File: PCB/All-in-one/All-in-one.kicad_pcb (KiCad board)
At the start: 4 copper layers, 61.9 x 55.5 mm, 81 parts, among them J1 HIGH VOLTAGE, J10 SWD, J2 LOW VOLTAGE, J3 Micro_SD_Card_Det, J4 USB_C_Receptacle_USB2.0, J5 GPIO, J6 Conn_01x02, J7 Conn_01x02, J8 I2C_EXT, J9 UART_EXT, Q1 AO3401A, SW1 SW_DP3T, SW2 SW_Push, SW3 BOOT, U1 TPS563201DDCR, U2 NCP114AMX330TCG, U3 STM32F401CDUx, U4 BMP280, U5 MPU-6050, U6 USBLC6-2P6, U7 MT9700, U8 MT9700, Y1 25MHz 12pF

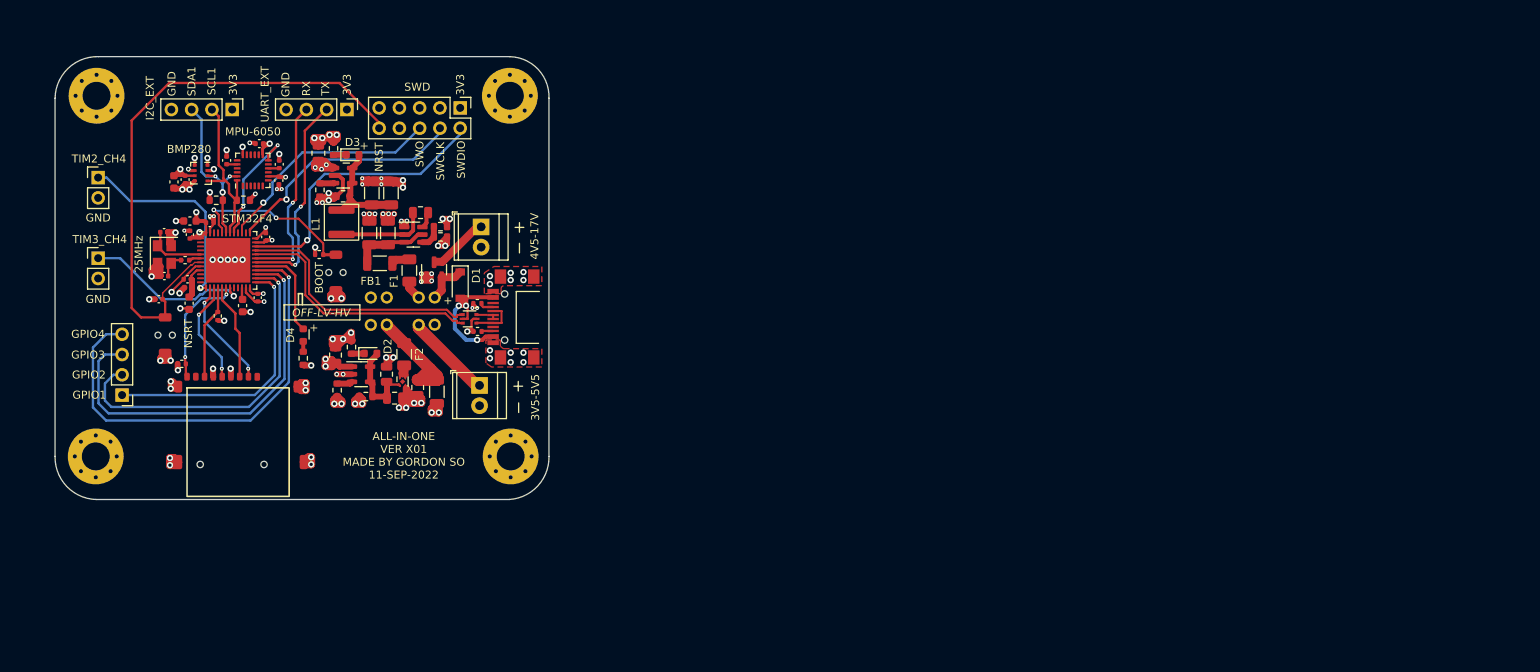
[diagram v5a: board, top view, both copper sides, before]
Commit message: Updated Circuit - Based on the new parts supplier LCSC, better components can be found - PCB is updated according to the new components
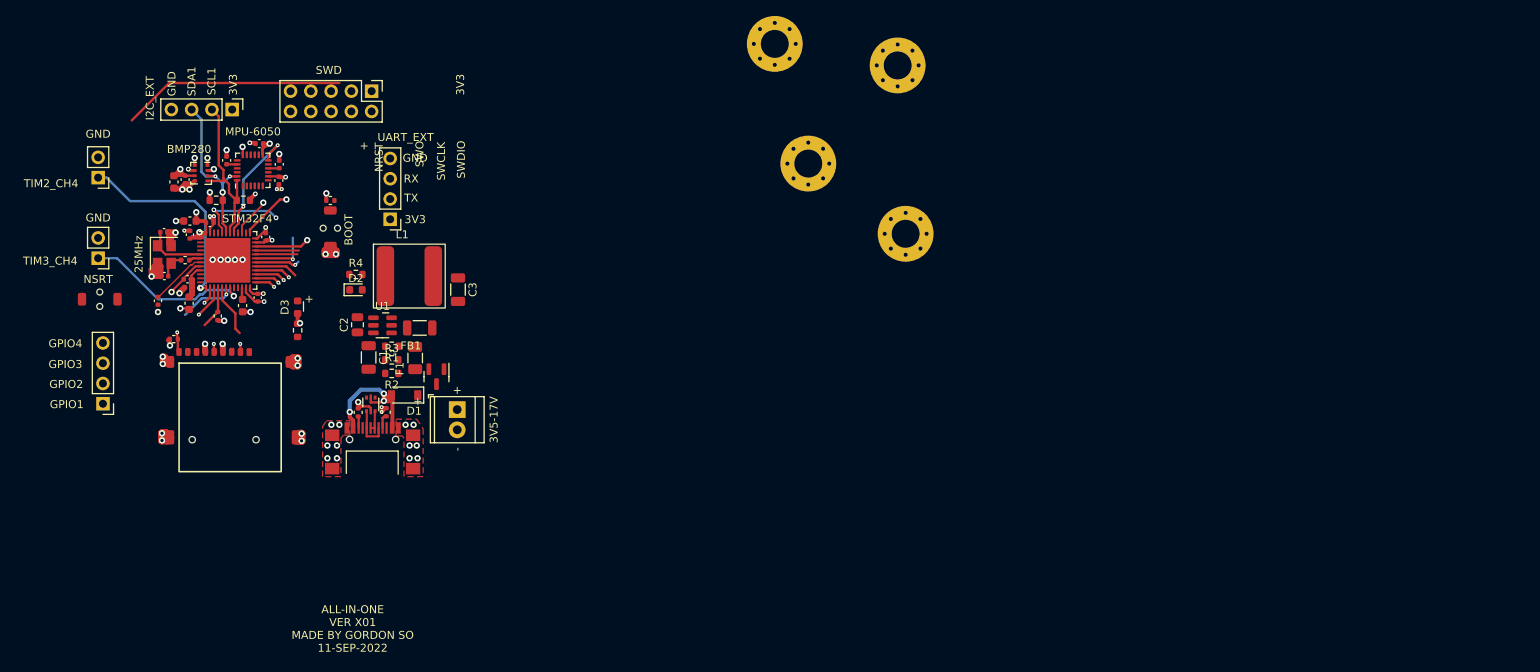
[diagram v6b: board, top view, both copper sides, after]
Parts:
- removed C26, C27, C28: 10u, Capacitor_SMD:C_0805_2012Metric
- removed the C4 at (59.5, 32.9)
- removed the C5 at (61.9, 32.9)
- removed the C6 at (67.7, 57.8)
- removed the C7 at (65.2, 57.2)
- removed the C8 at (62.4, 58.6)
- removed the D3 at (57.1, 28.1)
- removed F2: 250mA, Fuse:Fuse_1206_3216Metric
- removed the J2 at (73.0, 57.0)
- removed the R5 at (55.1, 57.6)
- removed the R6 at (54.7, 27.3)
- removed the R7 at (55.9, 33.3)
- removed the R8 at (53.0, 32.5)
- removed the SW1 at (67.4, 49.4)
- removed the U2 at (63.4, 56.5)
- removed U7, U8: MT9700, Package_TO_SOT_SMD:SOT-23-5
- C1: value 10u -> 22u
- C2: value 100n -> 1u; footprint Capacitor_SMD:C_1206_3216Metric -> Capacitor_SMD:C_0805_2012Metric
- C3: value 100n -> 22u; footprint Capacitor_SMD:C_0805_2012Metric -> Capacitor_SMD:C_1206_3216Metric
- D2: value LED_BLUE -> LED_RED
- L1: value 2u2 -> 22u; footprint All-in-one-custom:SMNR4020-2.2UH -> All-in-one-custom:MPIT8040
- R1: value 33.2k -> 75k
- R2: value 10k -> 40k2
- R3: value 1k5 -> 13k
- R4: value 10k -> 13k
- U1: value TPS563201DDCR -> TPMP1470
- moved H3 105.3 mm to (126.4, 38.0)
- moved H2 89.6 mm to (114.2, 29.2)
- moved H4 61.4 mm to (110.0, 14.2)
- moved H1 48.7 mm to (125.4, 16.9)
- moved J1 23.1 mm to (70.2, 60.0)
- moved J3 20.5 mm to (59.6, 62.3), turned to 0 degrees
- moved R2 18.2 mm to (62.0, 55.5)
- moved R13 18.1 mm to (57.8, 60.4), turned to 90 degrees
- moved R12 17.8 mm to (61.3, 60.4), turned to 90 degrees
- moved U5 16.4 mm to (59.4, 59.4), turned to 90 degrees
- moved R1 16.2 mm to (62.0, 52.1)
- moved C1 15.6 mm to (59.1, 53.5), turned to -90 degrees
- moved D1 15.4 mm to (63.6, 58.2), turned to 180 degrees
- moved R4 15.4 mm to (57.5, 43.1)
- moved J9 14.8 mm to (61.8, 36.2), turned to 180 degrees
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- renumbered C15 to C10, C16 to C11, C17 to C12, C18 to C13, C19 to C14, C20 to C15, C21 to C16, C22 to C17, C23 to C18, C24 to C19, C25 to C20, C9 to C4, C10 to C5, C11 to C6, C12 to C7, C13 to C8, C14 to C9, D4 to D3, J3 to J2, J4 to J3, J8 to J4, J10 to J6, J6 to J7, J7 to J8, R14 to R10, R15 to R11, R16 to R12, R17 to R13, R9 to R5, R10 to R6, R11 to R7, R12 to R8, R13 to R9, SW2 to SW1, SW3 to SW2, U3 to U2, U4 to U3, U5 to U4, U6 to U5
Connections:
- net BUCK_VIN renamed Net-(D1-Pad1)
- C2 pad 1: Net-(C1-Pad1) -> Net-(C2-Pad1)
- C2 pad 2: GND -> Net-(C2-Pad2)
- C3 pad 1: BUCK_SW -> +3.3V
- C3 pad 2: BUCK_VBST -> GND
- D2 pad 2: Net-(C26-Pad2) -> +3.3V
- L1 pad 1: BUCK_SW -> Net-(C2-Pad1)
- L1 pad 2: Net-(C4-Pad2) -> +3.3V
- R1 pad 1: +3.3V -> Net-(R1-Pad1)
- R1 pad 2: BUCK_VFB -> Net-(R1-Pad2)
- R2 pad 1: GND -> +3.3V
- R2 pad 2: BUCK_VFB -> Net-(R1-Pad2)
- R3 pad 1: GND -> Net-(R1-Pad2)
- R3 pad 2: Net-(D2-Pad1) -> GND
- R4 pad 1: GND -> Net-(D2-Pad1)
- R4 pad 2: Net-(C26-Pad2) -> GND
- U1 pad 2: BUCK_SW -> Net-(C2-Pad1)
- U1 pad 4: BUCK_VFB -> Net-(R1-Pad1)
- U1 pad 6: BUCK_VBST -> Net-(C2-Pad2)
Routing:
- net GND: track 163.1 -> 65.1 mm, vias 100 -> 53
- net NRST: track 73.4 -> 7.16 mm
- net GPIO_4: track 56.8 -> 4.55 mm
- net GPIO_3: track 50.5 -> 3.98 mm
- net GPIO_2: track 43.5 -> 3.33 mm
- net GPIO_1: track 33.9 -> 2.71 mm
- net SWDIO: track 35.8 -> 6.81 mm
- net unconnected-(J6-Pad7): track 0.00 -> 28.0 mm
- net USB_D-: track 32.1 -> 5.28 mm
- net USB_D+: track 32.1 -> 5.47 mm
- net LDO_IN: track 26.5 -> 0.00 mm
- net SWO: track 29.2 -> 5.00 mm
- net SWCLK: track 30.7 -> 6.56 mm
- net UART2_TX: track 26.6 -> 5.69 mm, vias 2 -> 1
- net UART2_RX: track 24.7 -> 7.44 mm, vias 2 -> 1
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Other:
- board outline removed
- board text added: "-"
- board text added: "3V5-17V"
- board text removed: "3V5-5V5"
- board text removed: "4V5-17V"
- board text removed: "OFF-LV-HV"

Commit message: PCB Tracing Update - Reroute traces
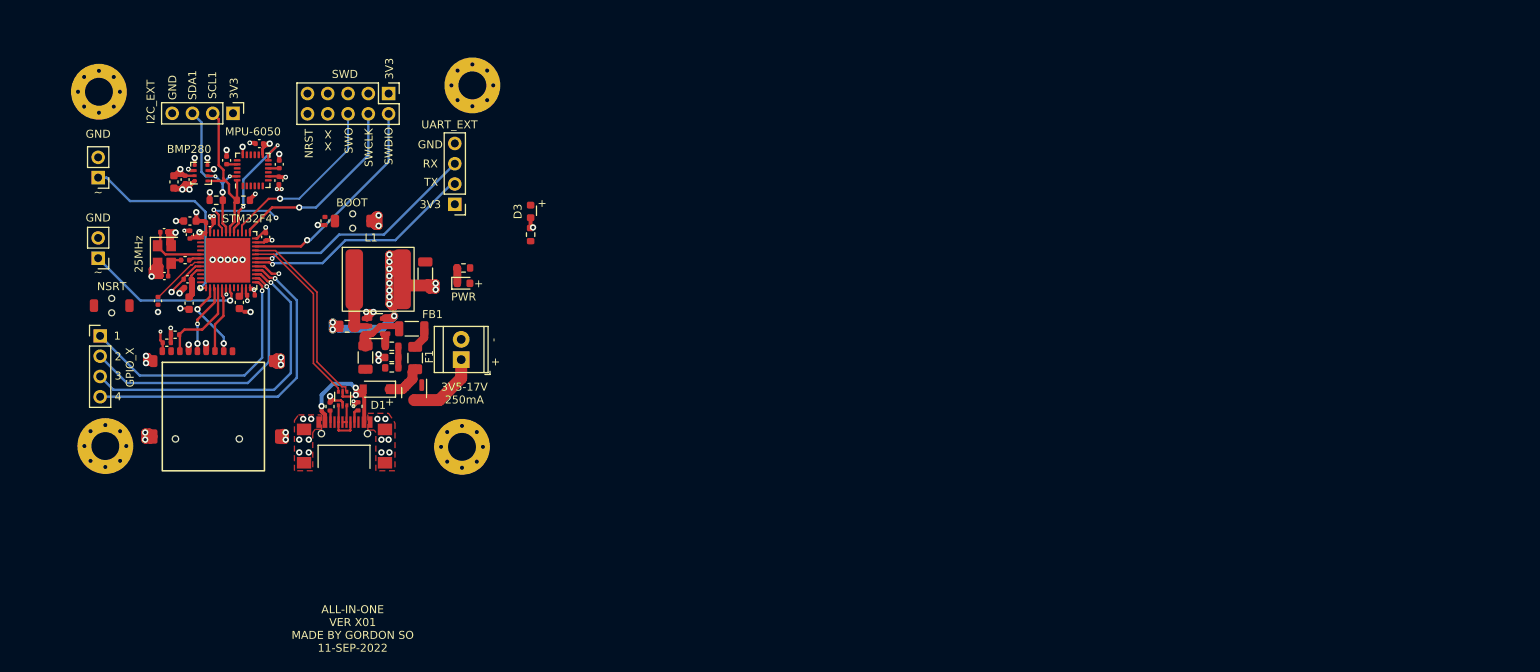
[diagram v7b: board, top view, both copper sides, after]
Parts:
- moved H2 94.9 mm to (26.1, 64.6)
- moved H4 84.9 mm to (25.3, 20.2)
- moved H3 61.7 mm to (70.8, 64.7)
- moved H1 53.4 mm to (72.1, 19.4)
- moved D3 31.6 mm to (79.4, 35.2)
- moved R7 31.6 mm to (79.4, 38.1)
- moved D2 13.5 mm to (71.0, 44.2)
- moved R4 13.5 mm to (71.0, 42.3)
- moved J5 8.51 mm to (25.4, 50.8), turned to 0 degrees
- moved J9 8.32 mm to (69.9, 34.3)
- moved J1 6.28 mm to (70.7, 53.8), turned to 90 degrees
- moved R8 5.83 mm to (34.9, 50.6), turned to 180 degrees
- moved C3 4.56 mm to (66.2, 43.0), turned to 90 degrees
- moved L1 3.92 mm to (60.3, 43.7)
- moved D1 3.61 mm to (60.1, 57.5)
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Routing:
- net GPIO_4: track 4.55 -> 42.1 mm
- net GPIO_3: track 3.98 -> 40.2 mm
- net GPIO_2: track 3.33 -> 35.1 mm
- net GPIO_1: track 2.71 -> 33.3 mm
- net +3.3V: track 37.5 -> 67.3 mm, vias 17 -> 28
- net unconnected-(J6-Pad7): track 28.0 -> 0.00 mm
- net UART2_TX: track 5.69 -> 29.3 mm
- net UART2_RX: track 7.44 -> 29.9 mm
- net SWDIO: track 6.81 -> 27.1 mm
- net USB_D+: track 5.47 -> 24.2 mm
- net SWCLK: track 6.56 -> 24.3 mm
- net SWO: track 5.00 -> 22.7 mm
- net USB_D-: track 5.28 -> 22.9 mm
- net Net-(C2-Pad2): track 0.00 -> 13.6 mm, vias 0 -> 3
- net +12V: track 0.00 -> 9.36 mm
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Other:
- board text added: "1"
- board text added: "2"
- board text added: "3"
- board text added: "3V5-17V 250mA"
- board text added: "4"
- board text added: "GPIO_X"
- board text added: "PWR"
- board text added: "X"
- board text added: "~"
- board text removed: "3V5-17V"
- board text removed: "GPIO1"
- board text removed: "GPIO2"
- board text removed: "GPIO3"
- board text removed: "GPIO4"

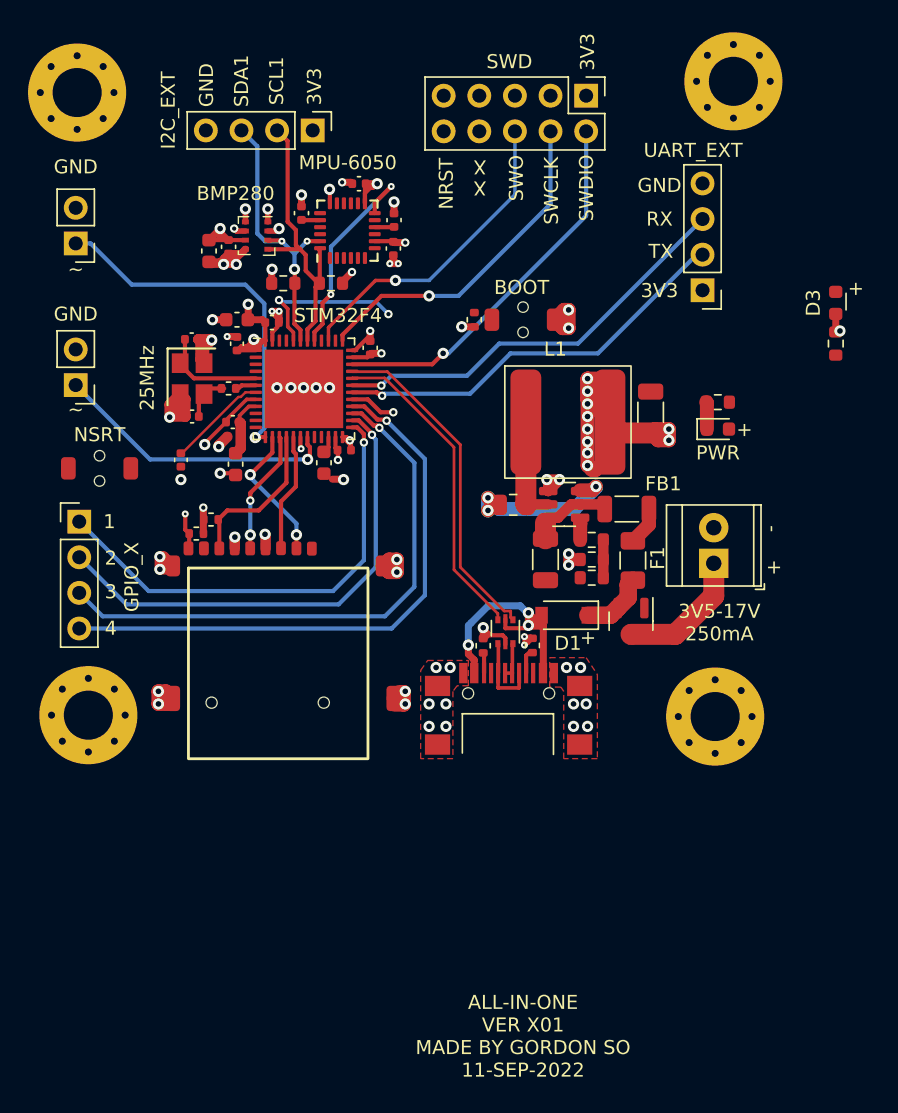
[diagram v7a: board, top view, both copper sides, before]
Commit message: PCB Update - PCB is good to go - Order is on hold as there maybe other projects that requires ordering
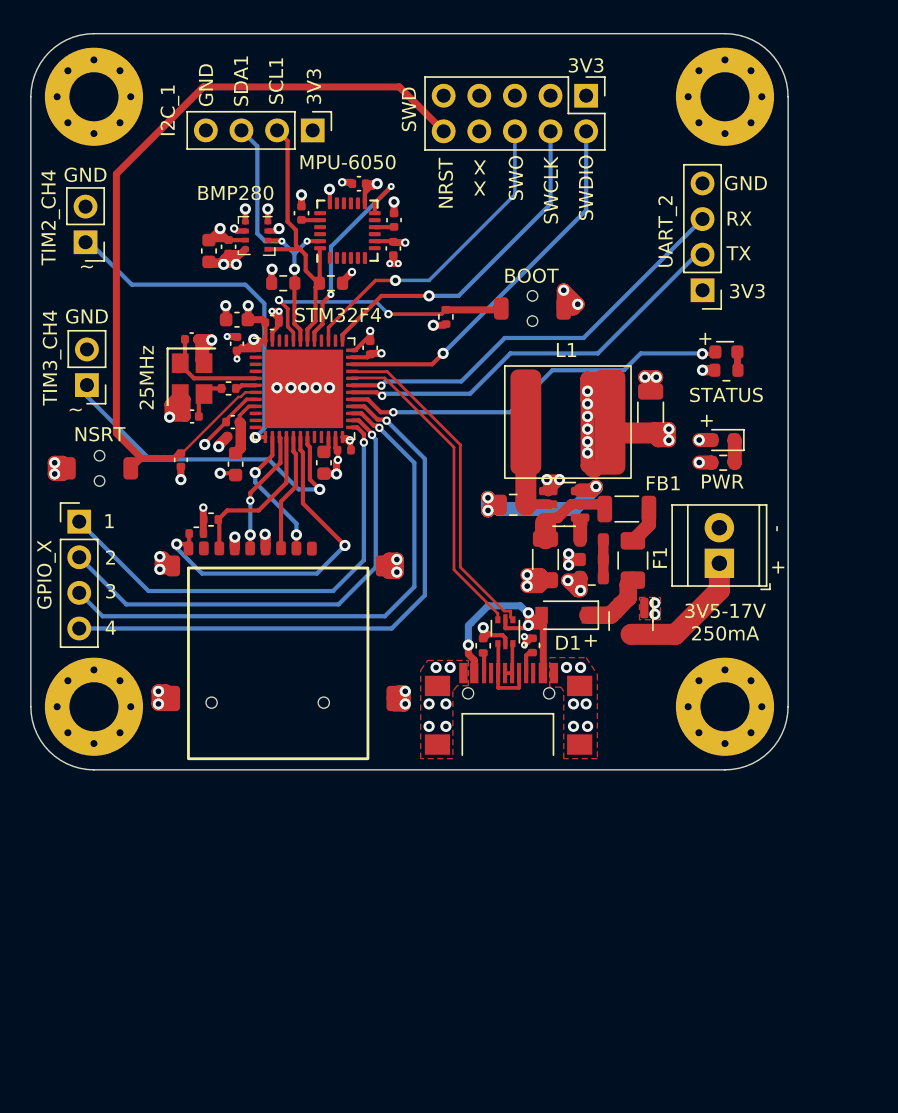
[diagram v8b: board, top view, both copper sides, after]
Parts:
- J4: value I2C_EXT -> I2C_1
- J9: value UART_EXT -> UART_2
- moved D3 8.55 mm to (71.6, 38.7), turned to 180 degrees
- moved R7 8.03 mm to (71.6, 40.0), turned to 180 degrees
- moved R4 4.34 mm to (71.4, 46.6), turned to 180 degrees
- moved R5 2.03 mm to (51.6, 36.2)
- moved H1 1.25 mm to (71.5, 20.5)
- moved H4 1.24 mm to (26.5, 20.5)
- moved SW2 1.05 mm to (57.8, 35.6)
- moved H3 0.99 mm to (71.5, 64.0)
- moved D2 0.86 mm to (71.4, 45.0), turned to 180 degrees
- moved J8 0.80 mm to (26.0, 41.1)
- moved H2 0.72 mm to (26.5, 64.0)
- moved J7 0.71 mm to (25.9, 30.9)
- moved J1 0.40 mm to (71.1, 53.8)
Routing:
- net NRST: track 7.16 -> 59.3 mm
- net LED_STATUS: track 3.32 -> 28.1 mm, vias 1 -> 2
- net SD_CARD_DET: track 3.80 -> 25.2 mm
- net GND: track 66.2 -> 81.6 mm, vias 55 -> 66
- net BOOT0: track 11.7 -> 19.9 mm
- net TIM3_CH4: track 20.5 -> 24.2 mm
- net +3.3V: track 67.3 -> 68.7 mm
- net TIM2_CH4: track 25.8 -> 25.1 mm
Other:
- board outline added: 54 x 52.5 mm
- board text added: "ALL-IN-ONE VER X01 MADE BY GORDON SO 16-SEP-2022"
- board text added: "STATUS"
- board text removed: "ALL-IN-ONE VER X01 MADE BY GORDON SO 11-SEP-2022"
